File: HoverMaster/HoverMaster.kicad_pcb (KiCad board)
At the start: 2 copper layers, 199.6 x 35 mm, 14 parts, among them J1 Conn_01x02_Male, J2 Conn_01x03_Male, J3 Conn_01x04_Male, J4 Conn_01x09, J5 Conn_01x03, J6 Conn_01x03, J7 Conn_01x03_Male, J8 Conn_01x03_Male, SW1 SW_Push, U1 NodeMCU_Amica_R2

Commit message: hovermaster
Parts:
- removed D1, D2: APA102, LED_SMD:LED_RGB_PLCC-6
- removed J1: Conn_01x02_Male, Connector_Phoenix_MSTB:PhoenixContact_MSTBVA_2,5_2-G_1x02_P5.00mm_Vertical
- removed J2, J8: Conn_01x03_Male, Connector_Phoenix_MSTB:PhoenixContact_MSTBVA_2,5_3-G-5,08_1x03_P5.08mm_Vertical
- removed J4: Conn_01x09, Connector_PinSocket_2.00mm:PinSocket_1x09_P2.00mm_Vertical
- removed J5, J6: Conn_01x03, Connector_PinSocket_2.00mm:PinSocket_1x03_P2.00mm_Vertical
- removed J7: Conn_01x03_Male, Connector_Phoenix_MSTB:PhoenixContact_MSTBVA_2,5_3-G_1x03_P5.00mm_Vertical
- removed SW1: SW_Push, Button_Switch_THT:SW_PUSH_6mm
- removed U1: NodeMCU_Amica_R2, nodemcu:NodeMCU_Amica_R2
- added BAT1: Conn_01x02_Male, Connector_Wire:SolderWirePad_1x02_P5.08mm_Drill1.5mm, F.Cu at (104.0, 149.0)
- added Bind1: SW_Push, Button_Switch_THT:SW_PUSH_6mm, F.Cu at (103.0, 159.2)
- added DCDC-12V1: DCDC-12V, Connector_Wire:SolderWirePad_1x03_P3.81mm_Drill1.2mm, F.Cu at (121.8, 129.0)
- added DCDC-5V1: Conn_01x03_Male, Connector_Wire:SolderWirePad_1x03_P3.81mm_Drill1.2mm, F.Cu at (109.5, 141.5)
- added Left_Sensor1: Conn_01x04, Connector_JST:JST_EH_B4B-EH-A_1x04_P2.50mm_Vertical, F.Cu at (96.5, 133.5)
- added Receiver_Power1: Conn_01x04, Connector_PinSocket_2.00mm:PinSocket_1x04_P2.00mm_Vertical, F.Cu at (93.0, 159.0)
- added Steering1: Conn_01x03_Male, Connector_Wire:SolderWirePad_1x03_P3.81mm_Drill1.2mm, F.Cu at (110.0, 129.0)
- J3: value Conn_01x04_Male -> LED; footprint Connector_Phoenix_MSTB:PhoenixContact_MSTBVA_2,5_4-G-5,08_1x04_P5.08mm_Vertical -> Connector_Wire:SolderWirePad_1x04_P3.81mm_Drill1.2mm
- moved J3 118.5 mm to (103.0, 117.8)
- moved F1 114.2 mm to (117.2, 137.5), turned to 270 degrees
- moved XA1 104.2 mm to (81.2, 117.5), turned to 180 degrees
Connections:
- XA1 pad 3V3: Net-(XA1-Pad3V3) -> (no net)
- XA1 pad A0: Net-(XA1-PadA0) -> (no net)
- XA1 pad A1: Net-(XA1-PadA1) -> (no net)
- XA1 pad A2: Net-(XA1-PadA2) -> (no net)
- XA1 pad A3: Net-(XA1-PadA3) -> (no net)
- XA1 pad A4: Net-(XA1-PadA4) -> (no net)
- XA1 pad A5: Net-(XA1-PadA5) -> (no net)
- XA1 pad A6: Net-(XA1-PadA6) -> (no net)
- XA1 pad A7: Net-(XA1-PadA7) -> (no net)
- XA1 pad AREF: Net-(XA1-PadAREF) -> (no net)
- XA1 pad D0: Net-(XA1-PadD0) -> (no net)
- XA1 pad D1: Net-(XA1-PadD1) -> (no net)
- XA1 pad D10: Signal_Steering -> (no net)
- XA1 pad D11: Signal_Light -> LED2
- XA1 pad D12: Net-(XA1-PadD12) -> LED1
- XA1 pad D13: Net-(XA1-PadD13) -> (no net)
- XA1 pad D2: C1 -> PPM_IN
- XA1 pad D3: C2 -> PPM_OUT
- XA1 pad D4: C3 -> (no net)
- XA1 pad D5: C4 -> (no net)
- XA1 pad D6: C5 -> (no net)
- XA1 pad D7: C6 -> (no net)
- XA1 pad D8: Status_D -> (no net)
- XA1 pad D9: Status_C -> (no net)
- XA1 pad GND1: Net-(XA1-PadGND1) -> (no net)
- XA1 pad RST1: Net-(XA1-PadRST1) -> (no net)
- XA1 pad RST2: Net-(XA1-PadRST2) -> (no net)
- XA1 pad VIN: Net-(XA1-PadVIN) -> (no net)
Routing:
- net GND: track 317.0 -> 97.2 mm, vias 0 -> 4
- net 5V: track 278.2 -> 70.0 mm, vias 4 -> 0
- net C10: track 123.3 -> 0.00 mm
- net C9: track 120.3 -> 0.00 mm
- net C8: track 117.2 -> 0.00 mm
- net C7: track 114.2 -> 0.00 mm
- net Signal_Steering: track 74.3 -> 0.00 mm, vias 2 -> 0
- net C1: track 57.4 -> 0.00 mm
- net C2: track 52.6 -> 0.00 mm
- net C3: track 49.2 -> 0.00 mm
- net C4: track 45.8 -> 0.00 mm
- net C5: track 42.5 -> 0.00 mm
- net S2: track 39.3 -> 0.00 mm, vias 2 -> 0
- net C6: track 39.1 -> 0.00 mm
- net S1: track 35.9 -> 0.00 mm, vias 2 -> 0
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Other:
- board size 199.6 x 35 mm -> 52.5 x 47 mm

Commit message: new routing
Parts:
- added J1: Conn_01x02_Male, Connector_Wire:SolderWirePad_1x02_P5.08mm_Drill1.5mm, F.Cu at (135.8, 140.2)
- added J2: Conn_01x02_Male, Connector_Wire:SolderWirePad_1x02_P5.08mm_Drill1.5mm, F.Cu at (130.5, 158.2)
- added K1: FRT5, Relay_THT:Relay_DPDT_FRT5, F.Cu at (127.0, 153.2)
- Left_Sensor1: value Conn_01x04 -> Conn_01x02; footprint Connector_JST:JST_EH_B4B-EH-A_1x04_P2.50mm_Vertical -> Connector_Wire:SolderWirePad_1x02_P3.81mm_Drill1.2mm
- moved DCDC-12V1 17.7 mm to (109.5, 141.8), turned to 90 degrees
- moved Steering1 10.1 mm to (100.5, 125.5)
- moved J3 8.50 mm to (94.5, 117.8)
- moved DCDC-5V1 6.75 mm to (102.8, 141.8)
- moved BAT1 6.15 mm to (109.5, 151.8), turned to 270 degrees
- moved Left_Sensor1 4.74 mm to (95.0, 138.0)
- moved F1 2.80 mm to (117.8, 134.8)
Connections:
- Left_Sensor1 pad 1: (no net) -> PPM_OUT
- Left_Sensor1 pad 2: (no net) -> GND
- XA1 pad D3: PPM_OUT -> HOVER_POWER_RELAY
- XA1 pad D4: (no net) -> PPM_OUT
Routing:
- net GND: track 97.2 -> 170.6 mm, vias 4 -> 0
- net HOVER_POWER_RELAY: track 0.00 -> 62.7 mm, vias 0 -> 2
- net 5V: track 70.0 -> 86.4 mm, vias 0 -> 4
- net LED2: track 14.8 -> 6.26 mm
- net 12V: track 4.19 -> 12.6 mm
- net LED1: track 15.3 -> 7.15 mm
- net Net-(J1-Pad2): track 0.00 -> 5.96 mm
- net Net-(J1-Pad1): track 0.00 -> 5.85 mm
- net BAT+: track 14.5 -> 8.74 mm
- net Net-(J2-Pad1): track 0.00 -> 5.65 mm
- net Net-(J2-Pad2): track 0.00 -> 5.40 mm
- net PPM_OUT: track 33.2 -> 30.0 mm
- net PPM_IN: track 12.5 -> 10.1 mm
- net (no net): track 18.1 -> 19.2 mm, vias 0 -> 4
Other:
- board size 52.5 x 47 mm -> 69.5 x 47 mm

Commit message: new controller design
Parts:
- removed Bind1: SW_Push, Button_Switch_THT:SW_PUSH_6mm
- removed DCDC-12V1: DCDC-12V, Connector_Wire:SolderWirePad_1x03_P3.81mm_Drill1.2mm
- removed Steering1: Conn_01x03_Male, Connector_Wire:SolderWirePad_1x03_P3.81mm_Drill1.2mm
- added R1: R, Resistor_THT:R_Axial_DIN0207_L6.3mm_D2.5mm_P2.54mm_Vertical, F.Cu at (97.0, 134.5)
- added R2: R, Resistor_THT:R_Axial_DIN0207_L6.3mm_D2.5mm_P2.54mm_Vertical, F.Cu at (102.2, 139.6)
- Receiver_Power1: footprint Connector_PinSocket_2.00mm:PinSocket_1x04_P2.00mm_Vertical -> Connector_PinSocket_2.00mm:PinSocket_1x03_P2.00mm_Vertical
- moved DCDC-5V1 13.7 mm to (109.8, 130.0), turned to 270 degrees
- moved Receiver_Power1 4.19 mm to (94.2, 155.0), turned to 0 degrees
- moved J3 3.80 mm to (98.2, 118.4)
- moved Left_Sensor1 2.85 mm to (97.2, 139.8)
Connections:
- Left_Sensor1 pad 1: PPM_OUT -> Net-(Left_Sensor1-Pad1)
- Receiver_Power1 pad 1: BIND -> PPM_IN
- Receiver_Power1 pad 2: 5V -> GND
- Receiver_Power1 pad 3: GND -> 5V
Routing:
- net GND: track 170.6 -> 139.8 mm
- net PPM_OUT: track 30.0 -> 13.2 mm, vias 2 -> 0
- net 5V: track 86.4 -> 102.2 mm, vias 4 -> 2
- net (no net): track 19.2 -> 34.8 mm
- net 12V: track 12.6 -> 0.00 mm
- net BIND: track 11.4 -> 0.00 mm
- net Net-(Left_Sensor1-Pad1): track 0.00 -> 11.3 mm
- net BAT_Fuse+: track 16.3 -> 8.39 mm
- net HOVER_POWER_RELAY: track 62.7 -> 55.5 mm
- net LED2: track 6.26 -> 10.3 mm
- net LED1: track 7.15 -> 11.2 mm
- net PPM_IN: track 10.1 -> 12.4 mm

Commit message: new master
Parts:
- added Hupe1: Conn_01x06_Male, Connector_JST:JST_EH_B6B-EH-A_1x06_P2.50mm_Vertical, F.Cu at (95.1, 135.4)
- added J4: Conn_01x03_Female, Connector_Wire:SolderWirePad_1x03_P3.81mm_Drill1.2mm, F.Cu at (114.0, 144.1)
- added Q1: BSS138, Package_TO_SOT_SMD:SOT-23, F.Cu at (100.8, 145.8)
- F1: footprint Fuse:Fuseholder_Cylinder-5x20mm_Stelvio-Kontek_PTF78_Horizontal_Open -> Fuse:Fuse_1812_4532Metric_Pad1.30x3.40mm_HandSolder
- J1, J2: footprint Connector_Wire:SolderWirePad_1x02_P5.08mm_Drill1.5mm -> Connector_JST:JST_EH_B2B-EH-A_1x02_P2.50mm_Vertical
- Left_Sensor1: value Conn_01x02 -> Conn_01x03; footprint Connector_Wire:SolderWirePad_1x02_P3.81mm_Drill1.2mm -> Connector_JST:JST_EH_B3B-EH-A_1x03_P2.50mm_Vertical
- R1, R2: value R -> 10K; footprint Resistor_THT:R_Axial_DIN0207_L6.3mm_D2.5mm_P2.54mm_Vertical -> Resistor_THT:R_Axial_DIN0204_L3.6mm_D1.6mm_P2.54mm_Vertical
- moved F1 18.8 mm to (114.2, 153.2), turned to 0 degrees
- moved J2 16.8 mm to (130.5, 141.5), turned to 90 degrees
- moved BAT1 15.8 mm to (125.2, 153.5), turned to 180 degrees
- moved R1 15.1 mm to (105.8, 146.8), turned to 90 degrees
- moved Left_Sensor1 14.1 mm to (105.8, 151.0)
- moved DCDC-5V1 13.8 mm to (121.6, 137.1), turned to 180 degrees
- moved R2 12.4 mm to (99.8, 151.8), turned to 90 degrees
- moved J3 7.87 mm to (106.1, 119.0)
- moved K1 5.35 mm to (130.2, 149.0), turned to 0 degrees
- moved J1 2.15 mm to (137.5, 139.0), turned to 270 degrees
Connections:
- Left_Sensor1 pad 1: Net-(Left_Sensor1-Pad1) -> 3.3V
- Left_Sensor1 pad 2: GND -> Net-(Left_Sensor1-Pad2)
- R1 pad 1: PPM_OUT -> 3.3V
- R1 pad 2: Net-(Left_Sensor1-Pad1) -> Net-(Left_Sensor1-Pad2)
- R2 pad 1: Net-(Left_Sensor1-Pad1) -> 5V
- R2 pad 2: GND -> PPM_OUT
- XA1 pad 3V3: (no net) -> 3.3V
- XA1 pad D6: (no net) -> Hupe_1
- XA1 pad D7: (no net) -> Hupe_2
- XA1 pad D8: (no net) -> Hupe_3
- XA1 pad D9: (no net) -> Hupe_4
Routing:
- net 3.3V: track 0.00 -> 72.3 mm
- net (no net): track 34.8 -> 0.00 mm, vias 4 -> 3
- net 5V: track 102.2 -> 71.2 mm, vias 2 -> 0
- net 12V: track 0.00 -> 22.5 mm
- net GND: track 139.8 -> 159.4 mm, vias 0 -> 1
- net Net-(J2-Pad2): track 5.40 -> 22.1 mm
- net Net-(Left_Sensor1-Pad2): track 0.00 -> 16.3 mm
- net Net-(J1-Pad1): track 5.85 -> 21.4 mm
- net BAT_Fuse+: track 8.39 -> 21.5 mm
- net Net-(Left_Sensor1-Pad1): track 11.3 -> 0.00 mm
- net Net-(J2-Pad1): track 5.65 -> 16.8 mm
- net HOVER_POWER_RELAY: track 55.5 -> 66.1 mm
- net LED2: track 10.3 -> 20.7 mm
- net Net-(J1-Pad2): track 5.96 -> 15.6 mm
- net LED1: track 11.2 -> 20.3 mm
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- added copper zone on B.Cu, net (none)
- added copper zone on F.Cu, net GND
- removed copper zone on B.Cu, net GND

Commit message: arduino
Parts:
- removed J4: Conn_01x03_Female, Connector_Wire:SolderWirePad_1x03_P3.81mm_Drill1.2mm
- added DCDC12V: Conn_01x03_Female, Connector_Phoenix_MC_HighVoltage:PhoenixContact_MCV_1,5_3-G-5.08_1x03_P5.08mm_Vertical, F.Cu at (112.5, 148.2)
- BAT1: footprint Connector_Wire:SolderWirePad_1x02_P5.08mm_Drill1.5mm -> Connector_Phoenix_MC_HighVoltage:PhoenixContact_MCV_1,5_2-G-5.08_1x02_P5.08mm_Vertical
- DCDC-5V1: footprint Connector_Wire:SolderWirePad_1x03_P3.81mm_Drill1.2mm -> Connector_Phoenix_MC_HighVoltage:PhoenixContact_MCV_1,5_3-G-5.08_1x03_P5.08mm_Vertical
- J3: footprint Connector_Wire:SolderWirePad_1x04_P3.81mm_Drill1.2mm -> Connector_Phoenix_MC_HighVoltage:PhoenixContact_MCV_1,5_4-G-5.08_1x04_P5.08mm_Vertical
- moved DCDC-5V1 28.3 mm to (102.9, 158.4), turned to 90 degrees
- moved J2 17.3 mm to (131.4, 158.8)
- moved J1 17.3 mm to (138.7, 156.2)
- moved R2 13.9 mm to (97.3, 138.0), turned to 0 degrees
- moved Left_Sensor1 13.8 mm to (94.7, 142.6)
- moved F1 9.72 mm to (123.1, 157.4), turned to 90 degrees
- moved K1 9.08 mm to (131.1, 140.0)
- moved BAT1 8.63 mm to (123.6, 145.0), turned to 270 degrees
- moved Q1 4.32 mm to (100.1, 141.5), turned to 90 degrees
- moved Hupe1 3.48 mm to (97.9, 133.3)
- moved R1 3.37 mm to (105.9, 143.4)
- moved J3 2.22 mm to (104.8, 120.8)
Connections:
- K1 pad 2: (no net) -> Net-(K1-Pad2)
- K1 pad 9: (no net) -> Net-(K1-Pad9)
- XA1 pad A0: (no net) -> Net-(XA1-PadA0)
- XA1 pad A1: (no net) -> Net-(XA1-PadA1)
- XA1 pad A2: (no net) -> Net-(XA1-PadA2)
- XA1 pad A3: (no net) -> Net-(XA1-PadA3)
- XA1 pad A4: (no net) -> Net-(XA1-PadA4)
- XA1 pad A5: (no net) -> Net-(XA1-PadA5)
- XA1 pad A6: (no net) -> Net-(XA1-PadA6)
- XA1 pad A7: (no net) -> Net-(XA1-PadA7)
- XA1 pad AREF: (no net) -> Net-(XA1-PadAREF)
- XA1 pad D0: (no net) -> Net-(XA1-PadD0)
- XA1 pad D1: (no net) -> Net-(XA1-PadD1)
- XA1 pad D10: (no net) -> Net-(XA1-PadD10)
- XA1 pad D13: (no net) -> Net-(XA1-PadD13)
- XA1 pad D5: (no net) -> Net-(XA1-PadD5)
- XA1 pad GND1: (no net) -> Net-(XA1-PadGND1)
- XA1 pad RST1: (no net) -> Net-(XA1-PadRST1)
- XA1 pad RST2: (no net) -> Net-(XA1-PadRST2)
- XA1 pad VIN: (no net) -> Net-(XA1-PadVIN)
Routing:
- net 12V: track 22.5 -> 64.7 mm
- net 3.3V: track 72.3 -> 56.1 mm, vias 0 -> 2
- net HOVER_POWER_RELAY: track 66.1 -> 54.2 mm, vias 2 -> 3
- net Net-(J1-Pad1): track 21.4 -> 10.5 mm
- net Net-(J2-Pad2): track 22.1 -> 11.4 mm
- net LED2: track 20.7 -> 29.4 mm
- net Net-(Left_Sensor1-Pad2): track 16.3 -> 24.5 mm
- net 5V: track 71.2 -> 63.8 mm
- net LED1: track 20.3 -> 26.0 mm
- net Hupe_4: track 7.69 -> 11.4 mm
- net Hupe_2: track 8.14 -> 11.4 mm
- net PPM_OUT: track 17.6 -> 14.4 mm
- net Hupe_3: track 8.28 -> 11.4 mm
- net Hupe_1: track 8.60 -> 11.4 mm
- net BAT_Fuse+: track 21.5 -> 23.7 mm
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- removed copper zone on B.Cu, net (none)
- removed copper zone on F.Cu, net GND
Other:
- outline, holes or cut-outs redrawn

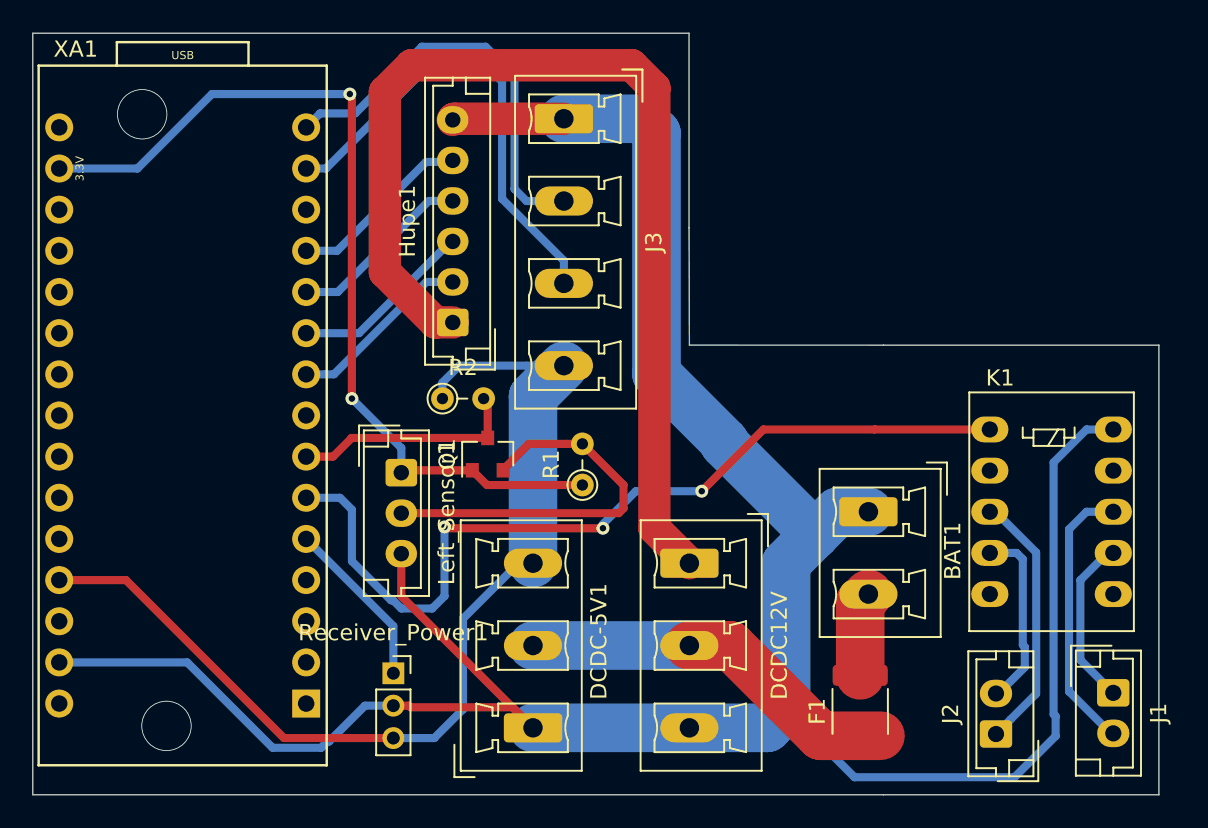
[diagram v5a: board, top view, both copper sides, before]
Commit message: added gnd plates
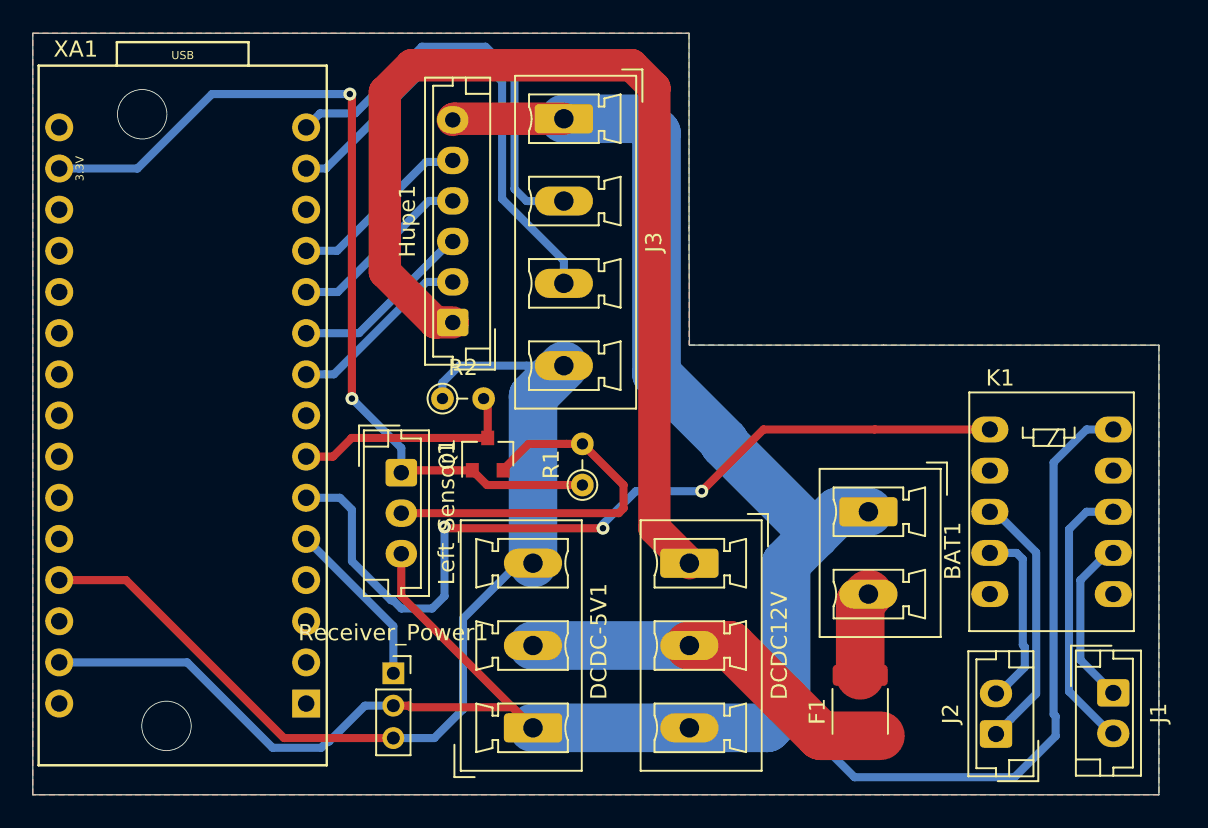
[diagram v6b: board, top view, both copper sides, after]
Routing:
- added copper zone on B.Cu, net GND
- added copper zone on F.Cu, net GND
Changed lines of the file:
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@@
   )
   (setup
-    (last_trace_width 0.5)
+    (last_trace_width 0.25)
     (user_trace_width 0.5)
     (user_trace_width 1)
@@
   (segment (start 108.458 143.383) (end 105.918 140.843) (width 0.5) (layer F.Cu) (net 20))
   (segment (start 108.458 144.827) (end 108.458 143.383) (width 0.5) (layer F.Cu) (net 20))
+  (zone (net 1) (net_name GND) (layer F.Cu) (hatch edge 0.508)
+    (connect_pads yes (clearance 0.508))
+    (min_thickness 0.254)
+    (fill yes (arc_segments 32) (thermal_gap 0.508) (thermal_bridge_width 0.508))
+    (polygon
+      (pts
+        (xy 72 115.5) (xy 112.5 115.5) (xy 112.5 134.75) (xy 141.5 134.75) (xy 141.5 162.5)
+        (xy 72 162.5)
+      )
+    )
+  )
+  (zone (net 1) (net_name GND) (layer B.Cu) (hatch edge 0.508)
+    (connect_pads (clearance 0.508))
+    (min_thickness 0.254)
+    (fill yes (arc_segments 32) (thermal_gap 0.508) (thermal_bridge_width 0.508))
+    (polygon
+      (pts
+        (xy 72 115.5) (xy 112.5 115.5) (xy 112.5 134.75) (xy 141.5 134.75) (xy 141.5 162.5)
+        (xy 72 162.5)
+      )
+    )
+  )
 )

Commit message: fixed missing ppm in filter resistor
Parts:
- added R3: 10kOhm, Resistor_SMD:R_1206_3216Metric_Pad1.42x1.75mm_HandSolder, F.Cu at (83.2, 146.7)
- Hupe1: footprint Connector_JST:JST_EH_B6B-EH-A_1x06_P2.50mm_Vertical -> Connector_JST:JST_EH_B06B-EH-A_1x06_P2.50mm_Vertical
- R1, R2: footprint Resistor_THT:R_Axial_DIN0204_L3.6mm_D1.6mm_P2.54mm_Vertical -> Resistor_SMD:R_1206_3216Metric_Pad1.42x1.75mm_HandSolder
- Receiver_Power1: footprint Connector_PinSocket_2.00mm:PinSocket_1x03_P2.00mm_Vertical -> Connector_JST:JST_EH_B03B-EH-A_1x03_P2.50mm_Vertical
- moved R1 1.78 mm to (106.0, 141.6)
- moved Receiver_Power1 1.38 mm to (94.6, 153.7), turned to 270 degrees
- moved R2 1.14 mm to (98.4, 138.0), turned to 180 degrees
- renumbered DCDC12V to J4
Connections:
- K1 pad 2: Net-(K1-Pad2) -> (no net)
- K1 pad 9: Net-(K1-Pad9) -> (no net)
- XA1 pad A0: Net-(XA1-PadA0) -> (no net)
- XA1 pad A1: Net-(XA1-PadA1) -> (no net)
- XA1 pad A2: Net-(XA1-PadA2) -> (no net)
- XA1 pad A3: Net-(XA1-PadA3) -> (no net)
- XA1 pad A4: Net-(XA1-PadA4) -> (no net)
- XA1 pad A5: Net-(XA1-PadA5) -> (no net)
- XA1 pad A6: Net-(XA1-PadA6) -> (no net)
- XA1 pad A7: Net-(XA1-PadA7) -> (no net)
- XA1 pad AREF: Net-(XA1-PadAREF) -> (no net)
- XA1 pad D0: Net-(XA1-PadD0) -> (no net)
- XA1 pad D1: Net-(XA1-PadD1) -> (no net)
- XA1 pad D10: Net-(XA1-PadD10) -> (no net)
- XA1 pad D13: Net-(XA1-PadD13) -> (no net)
- XA1 pad D5: Net-(XA1-PadD5) -> (no net)
- XA1 pad GND1: Net-(XA1-PadGND1) -> (no net)
- XA1 pad RST1: Net-(XA1-PadRST1) -> (no net)
- XA1 pad RST2: Net-(XA1-PadRST2) -> (no net)
- XA1 pad VIN: Net-(XA1-PadVIN) -> (no net)
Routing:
- net GND: track 161.4 -> 170.8 mm, vias 0 -> 3
- net HOVER_POWER_RELAY: track 54.2 -> 62.9 mm
- net PPM_IN: track 10.5 -> 14.8 mm
- net 3.3V: track 56.1 -> 57.6 mm
- net Net-(Left_Sensor1-Pad2): track 24.5 -> 25.7 mm
